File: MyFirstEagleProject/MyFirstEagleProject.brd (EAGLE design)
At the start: 75.9 x 50.8 mm, 6 parts

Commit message: Updated schematic/PCB files
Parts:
- removed IC1: (no value), ic-package:SOCKET-08
- removed LED1: (no value), led:CHIPLED_0805
- removed R1: (no value), SparkFun:R2010
- removed S1: (no value), switch-omron:B3F-10XX
- added 1K_RESISTOR_2010: (no value), SparkFun:R2010
- added ATTINY85: (no value), ic-package:SOCKET-08
- added LED_0805: (no value), led:CHIPLED_0805
- added OMRON_SWITCH: (no value), switch-omron:B3F-10XX
- moved +5V 1.80 mm to (71.1, 44.5)
- moved GND 1.80 mm to (62.2, 44.5)
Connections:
- removed net N$3: IC1.2, LED1.A
- new net N$1: ATTINY85.5, LED_0805.A
- net 5V: now also ATTINY85.8, OMRON_SWITCH.1, OMRON_SWITCH.2; no longer IC1.8, S1.1, S1.2
- net GND: now also 1K_RESISTOR_2010.1, ATTINY85.4, LED_0805.C; no longer IC1.4, LED1.C, R1.1
- net N$6: now also 1K_RESISTOR_2010.2, ATTINY85.6, OMRON_SWITCH.3, OMRON_SWITCH.4; no longer IC1.5, R1.2, S1.3, S1.4
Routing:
- net N$6: track 102.1 -> 27.9 mm
- net GND: track 59.9 -> 82.8 mm
- net N$1: track 0.00 -> 16.0 mm
- net N$3: track 10.9 -> 0.00 mm
- net 5V: track 53.1 -> 43.5 mm
- added copper zone on layer 1, net N$2
- removed copper zone on layer 1, net N$1
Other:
- board size 75.9 x 50.8 mm -> 77.1 x 50.8 mm

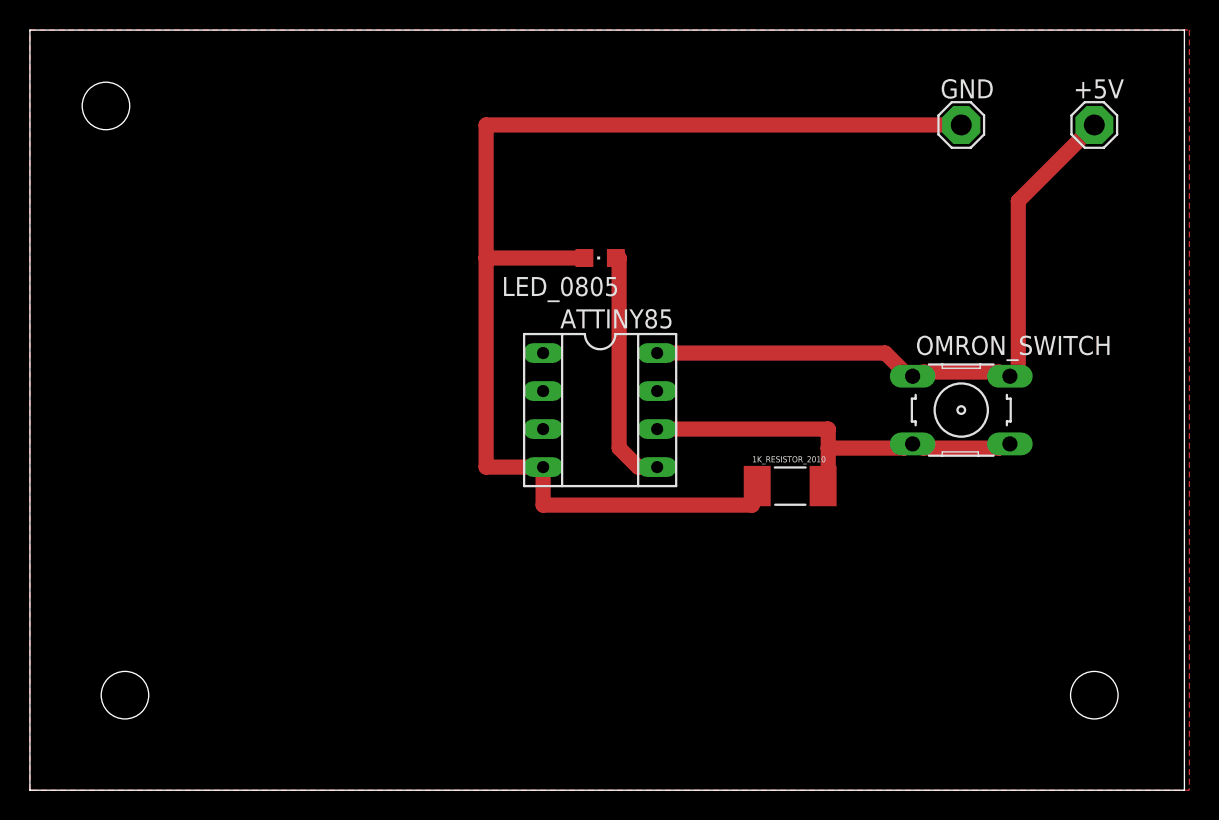
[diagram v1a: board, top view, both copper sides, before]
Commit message: Minor PCB fixes, added PCB layout for printing
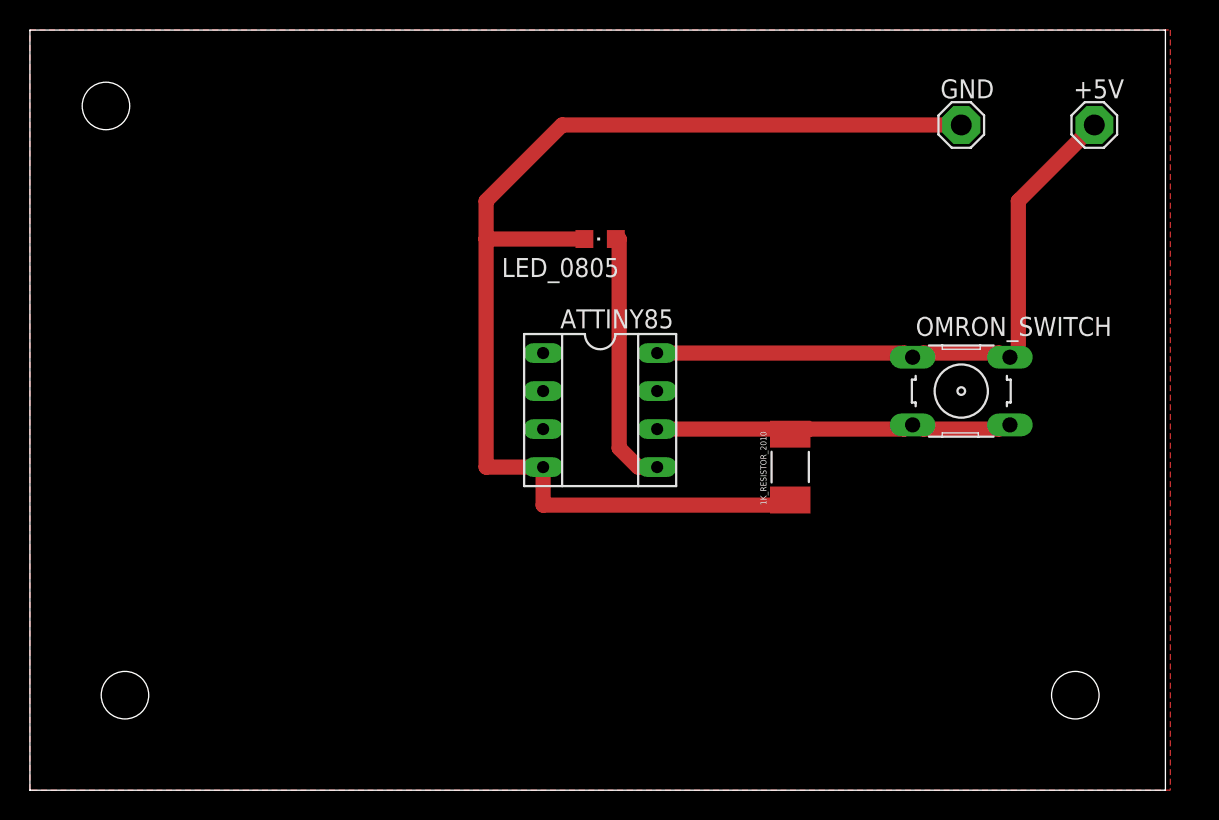
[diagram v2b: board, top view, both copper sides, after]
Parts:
- moved OMRON_SWITCH 1.27 mm to (62.2, 26.7)
- moved 1K_RESISTOR_2010 1.27 mm to (50.8, 21.6), turned to 90 degrees
- moved LED_0805 1.27 mm to (38.1, 36.8)
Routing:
- net N$6: track 27.9 -> 25.4 mm
- net 5V: track 43.5 -> 41.7 mm
- net GND: track 82.8 -> 81.4 mm
- net N$1: track 16.0 -> 17.3 mm
- added copper zone on layer 1, net GND
- removed copper zone on layer 1, net N$2
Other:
- board size 77.1 x 50.8 mm -> 75.9 x 50.8 mm
